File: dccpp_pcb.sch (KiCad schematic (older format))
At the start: 45 parts, among them J1 USB_B_Micro, J2 AVR-ISP-6, J3 OSTTC022162, J4 OSTTC022162, J5 OSTTC022162, U1 ATmega32U4-AU, U2 74HC04, U3 IFX007T, U4 IFX007T, U5 IFX007T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

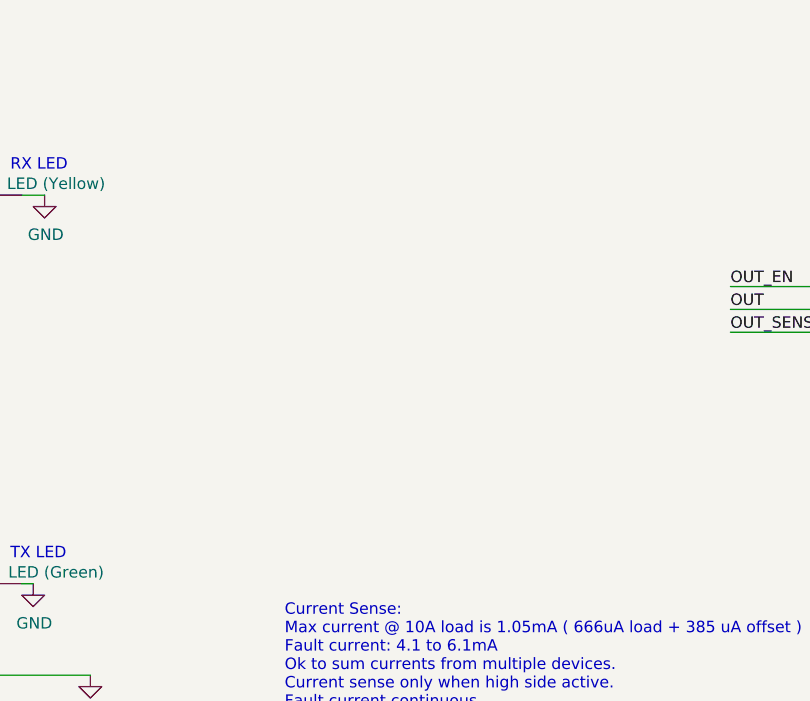
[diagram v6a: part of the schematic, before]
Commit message: Add digital connectors. Fixes most remaining ERC
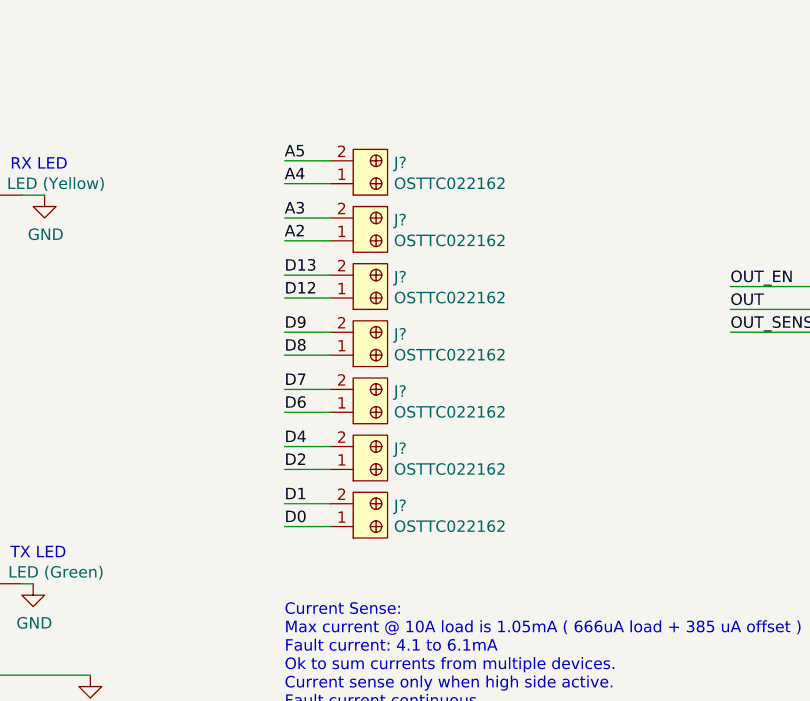
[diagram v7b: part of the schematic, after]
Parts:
- added J? (x7): OSTTC022162, digikey-footprints:Term_Block_1x2_P5.08MM, symbol dk_Terminal-Blocks-Wire-to-Board:OSTTC022162
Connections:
- net A2: now also J?.1
- net A3: now also J?.2
- net A4: now also J?.1
- net A5: now also J?.2
- net D0: now also J?.1
- net D1: now also J?.2
- net D12: now also J?.1
- net D13: now also J?.2
- net D2: now also J?.1
- net D4: now also J?.2
- net D6: now also J?.1
- net D7: now also J?.2
- net D8: now also J?.1
- net D9: now also J?.2
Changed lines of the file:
@@
 $EndComp
 Connection ~ 10250 900
+$Comp
+L dk_Terminal-Blocks-Wire-to-Board:OSTTC022162 J?
+U 1 1 5D4F1D7E
+P 5900 2750
+F 0 "J?" V 5991 2572 50  0000 R CNN
+F 1 "OSTTC022162" V 5900 2572 50  0000 R CNN
+F 2 "digikey-footprints:Term_Block_1x2_P5.08MM" H 6100 2950 60  0001 L CNN
+F 3 "http://www.on-shore.com/wp-content/uploads/OSTTCXX2162.pdf" H 6100 3050 60  0001 L CNN
+F 4 "ED2609-ND" H 6100 3150 60  0001 L CNN "Digi-Key_PN"
+F 5 "OSTTC022162" H 6100 3250 60  0001 L CNN "MPN"
+F 6 "Connectors, Interconnects" H 6100 3350 60  0001 L CNN "Category"
+F 7 "Terminal Blocks - Wire to Board" H 6100 3450 60  0001 L CNN "Family"
+F 8 "http://www.on-shore.com/wp-content/uploads/OSTTCXX2162.pdf" H 6100 3550 60  0001 L CNN "DK_Datasheet_Link"
+F 9 "/product-detail/en/on-shore-technology-inc/OSTTC022162/ED2609-ND/614558" H 6100 3650 60  0001 L CNN "DK_Detail_Page"
+F 10 "TERM BLK 2P SIDE ENT 5.08MM PCB" H 6100 3750 60  0001 L CNN "Description"
+F 11 "On Shore Technology Inc." H 6100 3850 60  0001 L CNN "Manufacturer"
+F 12 "Active" H 6100 3950 60  0001 L CNN "Status"
+	1    5900 2750
+	0    -1   -1   0
+$EndComp
+$Comp
+L dk_Terminal-Blocks-Wire-to-Board:OSTTC022162 J?
+U 1 1 5D4F5E05
+P 5900 2500
+F 0 "J?" V 5991 2322 50  0000 R CNN
+F 1 "OSTTC022162" V 5900 2322 50  0000 R CNN
+F 2 "digikey-footprints:Term_Block_1x2_P5.08MM" H 6100 2700 60  0001 L CNN
+F 3 "http://www.on-shore.com/wp-content/uploads/OSTTCXX2162.pdf" H 6100 2800 60  0001 L CNN
+F 4 "ED2609-ND" H 6100 2900 60  0001 L CNN "Digi-Key_PN"
+F 5 "OSTTC022162" H 6100 3000 60  0001 L CNN "MPN"
+F 6 "Connectors, Interconnects" H 6100 3100 60  0001 L CNN "Category"
+F 7 "Terminal Blocks - Wire to Board" H 6100 3200 60  0001 L CNN "Family"
+F 8 "http://www.on-shore.com/wp-content/uploads/OSTTCXX2162.pdf" H 6100 3300 60  0001 L CNN "DK_Datasheet_Link"
+F 9 "/product-detail/en/on-shore-technology-inc/OSTTC022162/ED2609-ND/614558" H 6100 3400 60  0001 L CNN "DK_Detail_Page"
+F 10 "TERM BLK 2P SIDE ENT 5.08MM PCB" H 6100 3500 60  0001 L CNN "Description"
+F 11 "On Shore Technology Inc." H 6100 3600 60  0001 L CNN "Manufacturer"
+F 12 "Active" H 6100 3700 60  0001 L CNN "Status"
+	1    5900 2500
+	0    -1   -1   0
+$EndComp
+$Comp
+L dk_Terminal-Blocks-Wire-to-Board:OSTTC022162 J?
+U 1 1 5D4F65A0
+P 5900 2250
+F 0 "J?" V 5991 2072 50  0000 R CNN
+F 1 "OSTTC022162" V 5900 2072 50  0000 R CNN
+F 2 "digikey-footprints:Term_Block_1x2_P5.08MM" H 6100 2450 60  0001 L CNN
+F 3 "http://www.on-shore.com/wp-content/uploads/OSTTCXX2162.pdf" H 6100 2550 60  0001 L CNN
+F 4 "ED2609-ND" H 6100 2650 60  0001 L CNN "Digi-Key_PN"
+F 5 "OSTTC022162" H 6100 2750 60  0001 L CNN "MPN"
+F 6 "Connectors, Interconnects" H 6100 2850 60  0001 L CNN "Category"
+F 7 "Terminal Blocks - Wire to Board" H 6100 2950 60  0001 L CNN "Family"
+F 8 "http://www.on-shore.com/wp-content/uploads/OSTTCXX2162.pdf" H 6100 3050 60  0001 L CNN "DK_Datasheet_Link"
+F 9 "/product-detail/en/on-shore-technology-inc/OSTTC022162/ED2609-ND/614558" H 6100 3150 60  0001 L CNN "DK_Detail_Page"
+F 10 "TERM BLK 2P SIDE ENT 5.08MM PCB" H 6100 3250 60  0001 L CNN "Description"
+F 11 "On Shore Technology Inc." H 6100 3350 60  0001 L CNN "Manufacturer"
+F 12 "Active" H 6100 3450 60  0001 L CNN "Status"
+	1    5900 2250
+	0    -1   -1   0
+$EndComp
+$Comp
+L dk_Terminal-Blocks-Wire-to-Board:OSTTC022162 J?
+U 1 1 5D4F6D61
+P 5900 2000
+F 0 "J?" V 5991 1822 50  0000 R CNN
+F 1 "OSTTC022162" V 5900 1822 50  0000 R CNN
+F 2 "digikey-footprints:Term_Block_1x2_P5.08MM" H 6100 2200 60  0001 L CNN
+F 3 "http://www.on-shore.com/wp-content/uploads/OSTTCXX2162.pdf" H 6100 2300 60  0001 L CNN
+F 4 "ED2609-ND" H 6100 2400 60  0001 L CNN "Digi-Key_PN"
+F 5 "OSTTC022162" H 6100 2500 60  0001 L CNN "MPN"
+F 6 "Connectors, Interconnects" H 6100 2600 60  0001 L CNN "Category"
+F 7 "Terminal Blocks - Wire to Board" H 6100 2700 60  0001 L CNN "Family"
+F 8 "http://www.on-shore.com/wp-content/uploads/OSTTCXX2162.pdf" H 6100 2800 60  0001 L CNN "DK_Datasheet_Link"
+F 9 "/product-detail/en/on-shore-technology-inc/OSTTC022162/ED2609-ND/614558" H 6100 2900 60  0001 L CNN "DK_Detail_Page"
+F 10 "TERM BLK 2P SIDE ENT 5.08MM PCB" H 6100 3000 60  0001 L CNN "Description"
+F 11 "On Shore Technology Inc." H 6100 3100 60  0001 L CNN "Manufacturer"
+F 12 "Active" H 6100 3200 60  0001 L CNN "Status"
+	1    5900 2000
+	0    -1   -1   0
+$EndComp
+$Comp
+L dk_Terminal-Blocks-Wire-to-Board:OSTTC022162 J?
+U 1 1 5D4F7430
+P 5900 1750
+F 0 "J?" V 5991 1572 50  0000 R CNN
+F 1 "OSTTC022162" V 5900 1572 50  0000 R CNN
+F 2 "digikey-footprints:Term_Block_1x2_P5.08MM" H 6100 1950 60  0001 L CNN
+F 3 "http://www.on-shore.com/wp-content/uploads/OSTTCXX2162.pdf" H 6100 2050 60  0001 L CNN
+F 4 "ED2609-ND" H 6100 2150 60  0001 L CNN "Digi-Key_PN"
+F 5 "OSTTC022162" H 6100 2250 60  0001 L CNN "MPN"
+F 6 "Connectors, Interconnects" H 6100 2350 60  0001 L CNN "Category"
+F 7 "Terminal Blocks - Wire to Board" H 6100 2450 60  0001 L CNN "Family"
+F 8 "http://www.on-shore.com/wp-content/uploads/OSTTCXX2162.pdf" H 6100 2550 60  0001 L CNN "DK_Datasheet_Link"
+F 9 "/product-detail/en/on-shore-technology-inc/OSTTC022162/ED2609-ND/614558" H 6100 2650 60  0001 L CNN "DK_Detail_Page"
+F 10 "TERM BLK 2P SIDE ENT 5.08MM PCB" H 6100 2750 60  0001 L CNN "Description"
+F 11 "On Shore Technology Inc." H 6100 2850 60  0001 L CNN "Manufacturer"
+F 12 "Active" H 6100 2950 60  0001 L CNN "Status"
+	1    5900 1750
+	0    -1   -1   0
+$EndComp
+$Comp
+L dk_Terminal-Blocks-Wire-to-Board:OSTTC022162 J?
+U 1 1 5D4F80FF
+P 5900 1500
+F 0 "J?" V 5991 1322 50  0000 R CNN
+F 1 "OSTTC022162" V 5900 1322 50  0000 R CNN
+F 2 "digikey-footprints:Term_Block_1x2_P5.08MM" H 6100 1700 60  0001 L CNN
+F 3 "http://www.on-shore.com/wp-content/uploads/OSTTCXX2162.pdf" H 6100 1800 60  0001 L CNN
+F 4 "ED2609-ND" H 6100 1900 60  0001 L CNN "Digi-Key_PN"
+F 5 "OSTTC022162" H 6100 2000 60  0001 L CNN "MPN"
+F 6 "Connectors, Interconnects" H 6100 2100 60  0001 L CNN "Category"
+F 7 "Terminal Blocks - Wire to Board" H 6100 2200 60  0001 L CNN "Family"
+F 8 "http://www.on-shore.com/wp-content/uploads/OSTTCXX2162.pdf" H 6100 2300 60  0001 L CNN "DK_Datasheet_Link"
+F 9 "/product-detail/en/on-shore-technology-inc/OSTTC022162/ED2609-ND/614558" H 6100 2400 60  0001 L CNN "DK_Detail_Page"
+F 10 "TERM BLK 2P SIDE ENT 5.08MM PCB" H 6100 2500 60  0001 L CNN "Description"
+F 11 "On Shore Technology Inc." H 6100 2600 60  0001 L CNN "Manufacturer"
+F 12 "Active" H 6100 2700 60  0001 L CNN "Status"
+	1    5900 1500
+	0    -1   -1   0
+$EndComp
+Text Label 5600 2750 0    50   ~ 0
+D0
+Text Label 5600 2650 0    50   ~ 0
+D1
+Text Label 5600 2500 0    50   ~ 0
+D2
+Text Label 5600 2400 0    50   ~ 0
+D4
+Text Label 5600 2250 0    50   ~ 0
+D6
+Text Label 5600 2150 0    50   ~ 0
+D7
+Text Label 5600 2000 0    50   ~ 0
+D8
+Text Label 5600 1900 0    50   ~ 0
+D9
+Text Label 5600 1750 0    50   ~ 0
+D12
+Text Label 5600 1650 0    50   ~ 0
+D13
+Text Label 5600 1500 0    50   ~ 0
+A2
+Text Label 5600 1400 0    50   ~ 0
+A3
+Text Label 5600 1250 0    50   ~ 0
+A4
+Text Label 5600 1150 0    50   ~ 0
+A5
+$Comp
+L dk_Terminal-Blocks-Wire-to-Board:OSTTC022162 J?
+U 1 1 5D508A0B
+P 5900 1250
+F 0 "J?" V 5991 1072 50  0000 R CNN
+F 1 "OSTTC022162" V 5900 1072 50  0000 R CNN
+F 2 "digikey-footprints:Term_Block_1x2_P5.08MM" H 6100 1450 60  0001 L CNN
+F 3 "http://www.on-shore.com/wp-content/uploads/OSTTCXX2162.pdf" H 6100 1550 60  0001 L CNN
+F 4 "ED2609-ND" H 6100 1650 60  0001 L CNN "Digi-Key_PN"
+F 5 "OSTTC022162" H 6100 1750 60  0001 L CNN "MPN"
+F 6 "Connectors, Interconnects" H 6100 1850 60  0001 L CNN "Category"
+F 7 "Terminal Blocks - Wire to Board" H 6100 1950 60  0001 L CNN "Family"
+F 8 "http://www.on-shore.com/wp-content/uploads/OSTTCXX2162.pdf" H 6100 2050 60  0001 L CNN "DK_Datasheet_Link"
+F 9 "/product-detail/en/on-shore-technology-inc/OSTTC022162/ED2609-ND/614558" H 6100 2150 60  0001 L CNN "DK_Detail_Page"
+F 10 "TERM BLK 2P SIDE ENT 5.08MM PCB" H 6100 2250 60  0001 L CNN "Description"
+F 11 "On Shore Technology Inc." H 6100 2350 60  0001 L CNN "Manufacturer"
+F 12 "Active" H 6100 2450 60  0001 L CNN "Status"
+	1    5900 1250
+	0    -1   -1   0
+$EndComp
+Wire Wire Line
+	5600 1150 5800 1150
+Wire Wire Line
+	5800 1250 5600 1250
+Wire Wire Line
+	5600 1400 5800 1400
+Wire Wire Line
+	5800 1500 5600 1500
+Wire Wire Line
+	5600 1650 5800 1650
+Wire Wire Line
+	5800 1750 5600 1750
+Wire Wire Line
+	5600 1900 5800 1900
+Wire Wire Line
+	5800 2000 5600 2000
+Wire Wire Line
+	5600 2150 5800 2150
+Wire Wire Line
+	5800 2250 5600 2250
+Wire Wire Line
+	5600 2400 5800 2400
+Wire Wire Line
+	5800 2500 5600 2500
+Wire Wire Line
+	5600 2650 5800 2650
+Wire Wire Line
+	5800 2750 5600 2750
 $EndSCHEMATC

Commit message: Assign most footprints
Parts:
- added R20: 10k, Resistor_SMD:R_0603_1608Metric_Pad1.05x0.95mm_HandSolder, symbol Device:R_Small_US
- C10, C11, C2, C3, C4, C5, C6, C7, C8, C9: footprint (none) -> Capacitor_SMD:C_0603_1608Metric_Pad1.05x0.95mm_HandSolder
- D1, D2: footprint (none) -> LED_SMD:LED_0603_1608Metric_Pad1.05x0.95mm_HandSolder
- J2: footprint (none) -> Connector_IDC:IDC-Header_2x03_P2.54mm_Vertical
- R1, R10, R11, R12, R13, R14, R15, R16, R17, R18, R19, R2, R3, R4, R5, R6, R7, R8, R9: footprint (none) -> Resistor_SMD:R_0603_1608Metric_Pad1.05x0.95mm_HandSolder
- U3, U4, U5, U6: footprint (none) -> Package_TO_SOT_SMD:TO-263-7_TabPin8
- gave numbers to parts that had none: 7
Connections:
- net GND: now also R20.1; no longer U1.33 (~HWB~/PE2)
- new net: R20.2, U1.33 (~HWB~/PE2)
